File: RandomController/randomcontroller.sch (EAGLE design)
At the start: 96 parts, among them IC1 TPS2054B, IC2 TPS2054B, IC3 TPS2054B, IC4 PIC16F1939PT, IC5 TPS2054B, Q1 NX-3215, U1 MCP1700_SOT23

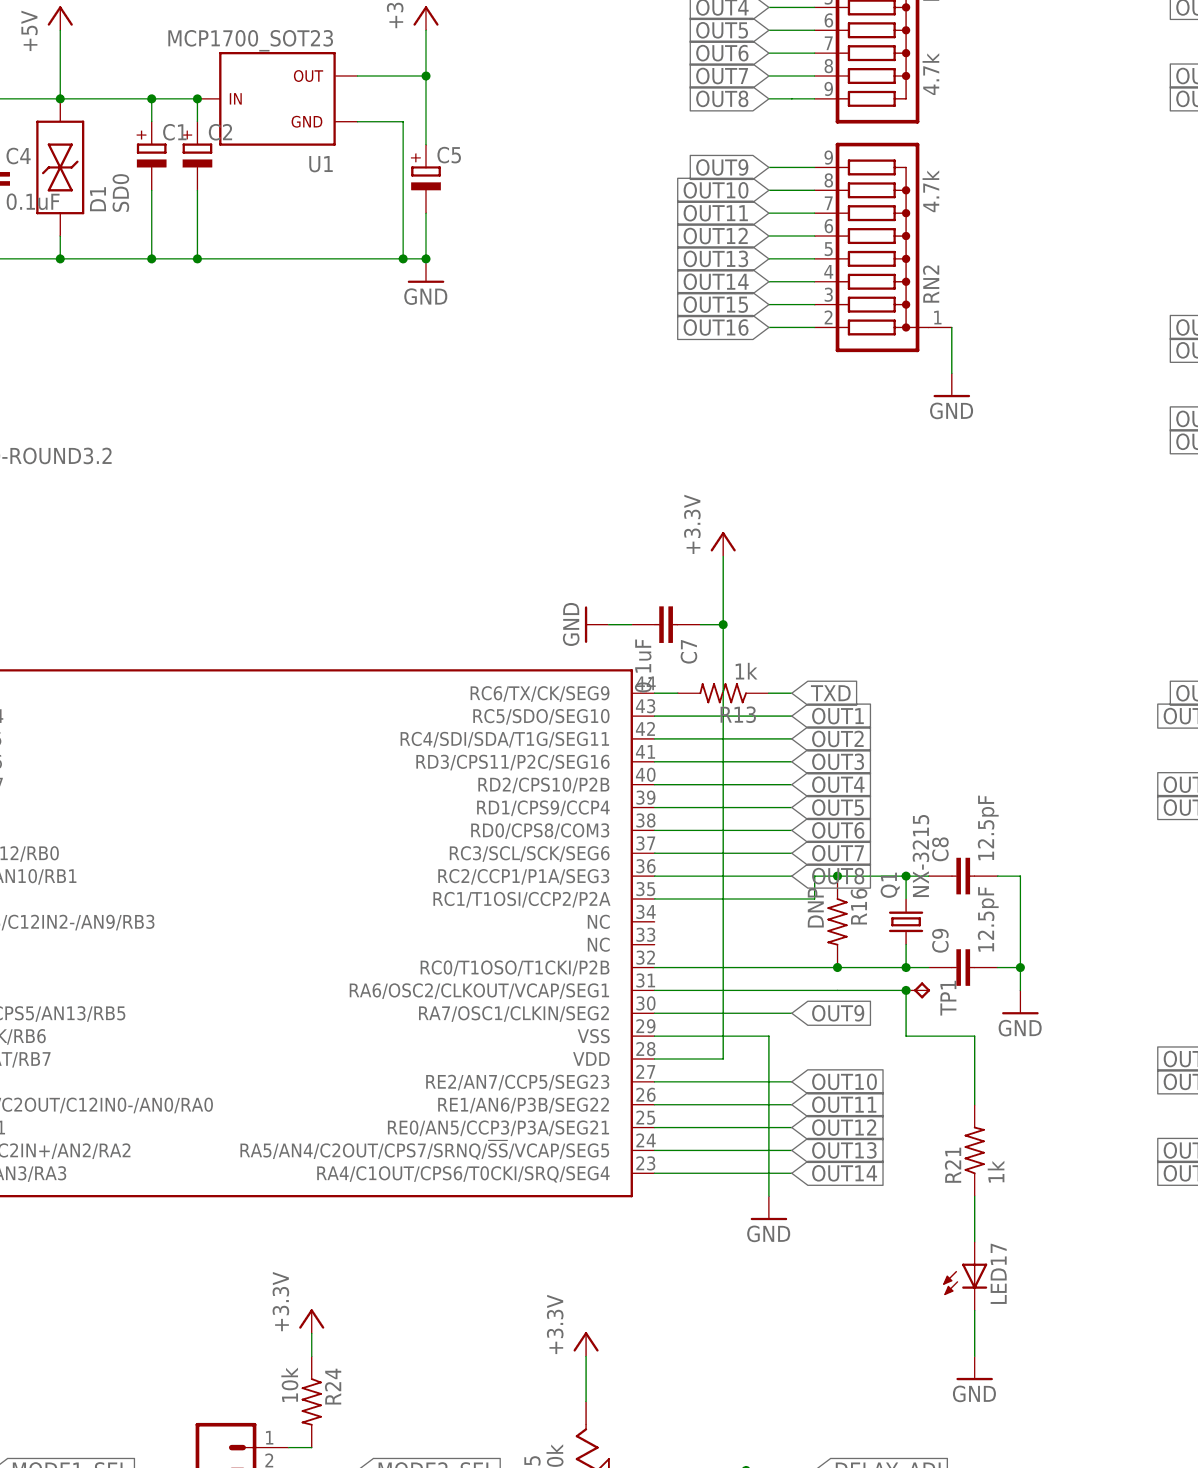
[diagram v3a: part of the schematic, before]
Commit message: part list added
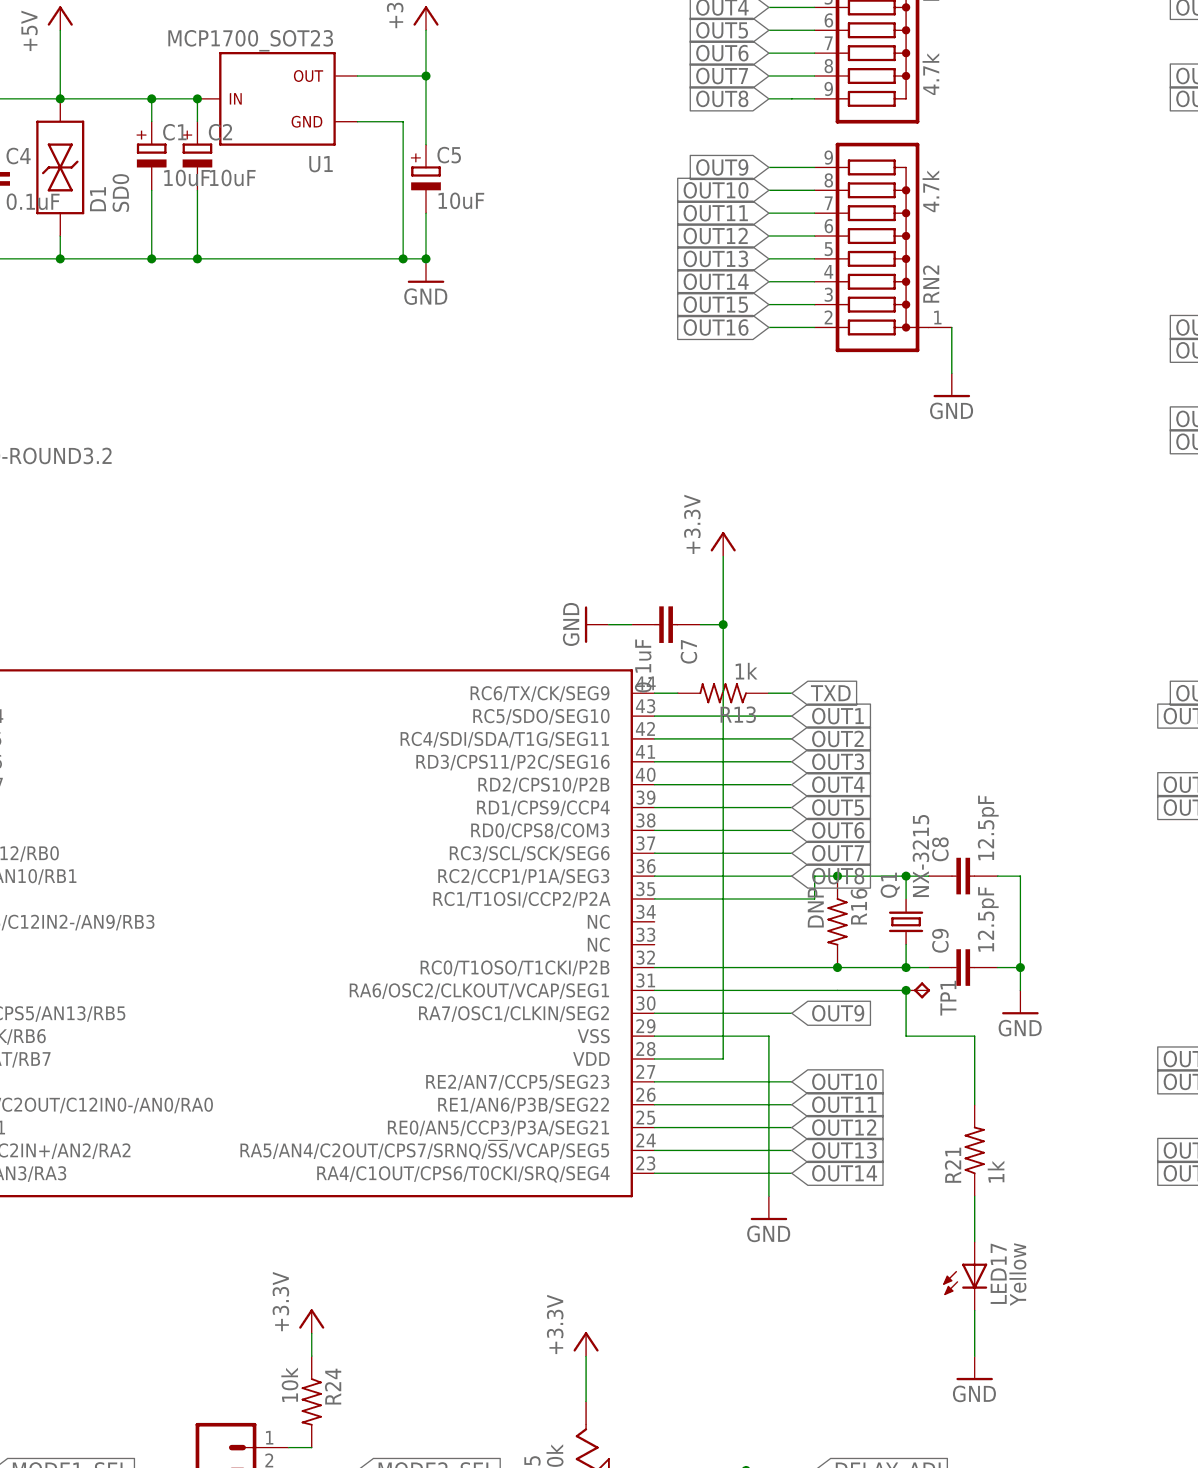
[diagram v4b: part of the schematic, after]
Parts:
- C1, C2, C5: value (none) -> 10uF
- LED17: value (none) -> Yellow
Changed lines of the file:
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@@
 <part name="U1" library="OSSI" deviceset="MCP1700" device="_SOT23"/>
 <part name="D1" library="WaterDrop" deviceset="SD0" device=""/>
-<part name="C1" library="yBrainDigital" deviceset="C-TANTAL-A" device=""/>
-<part name="C5" library="yBrainDigital" deviceset="C-TANTAL-A" device=""/>
+<part name="C1" library="yBrainDigital" deviceset="C-TANTAL-A" device="" value="10uF"/>
+<part name="C5" library="yBrainDigital" deviceset="C-TANTAL-A" device="" value="10uF"/>
 <part name="OK1" library="optocoupler" deviceset="4N*?M" device="S" technology="35"/>
 <part name="D2" library="WaterDrop" deviceset="SD0" device=""/>
@@
 <part name="STRUT_GND2" library="WaterDrop" deviceset="STRUT_GND" device=""/>
 <part name="C4" library="WaterDrop" deviceset="C" device="0805(2012)" value="0.1uF"/>
-<part name="C2" library="yBrainDigital" deviceset="C-TANTAL-A" device=""/>
+<part name="C2" library="yBrainDigital" deviceset="C-TANTAL-A" device="" value="10uF"/>
 <part name="R21" library="WaterDrop" deviceset="R" device="0805(2012)" value="1k"/>
-<part name="LED17" library="adafruit" deviceset="LED" device="CHIPLED_0805"/>
+<part name="LED17" library="adafruit" deviceset="LED" device="CHIPLED_0805" value="Yellow"/>
 <part name="GND54" library="supply1" deviceset="GND" device=""/>
 <part name="U$1" library="WaterDrop" deviceset="LOGO" device=""/>
